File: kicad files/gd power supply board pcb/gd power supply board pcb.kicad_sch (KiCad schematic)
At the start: 16 parts

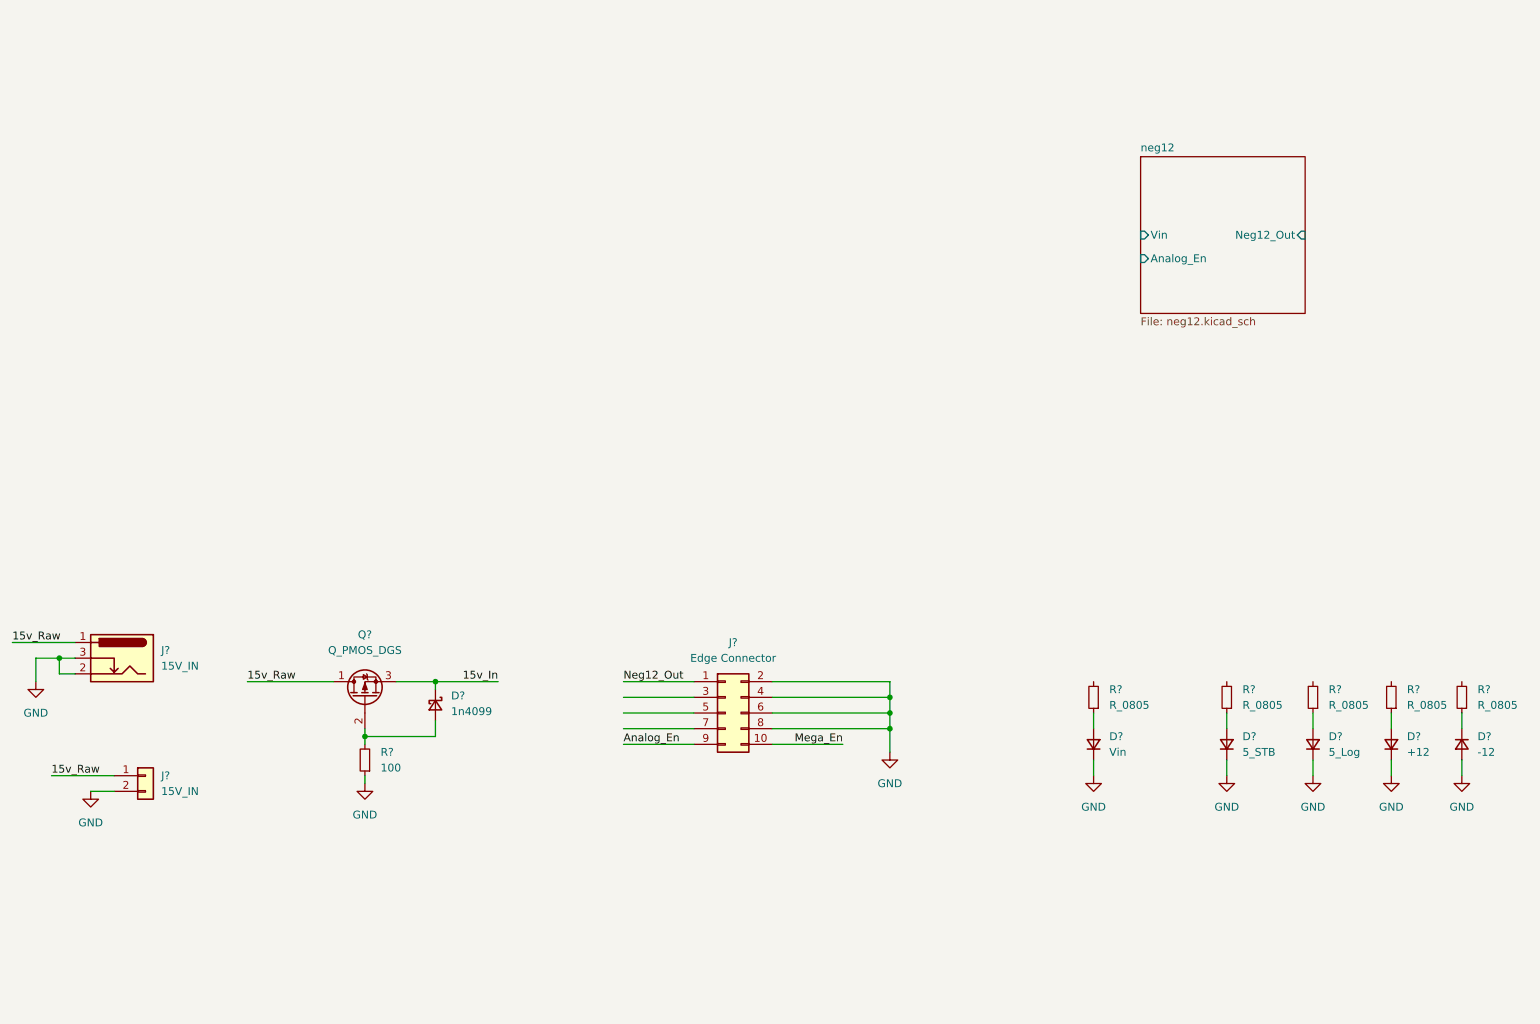
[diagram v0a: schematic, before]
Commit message: added 12v circuit with 34063 switcher
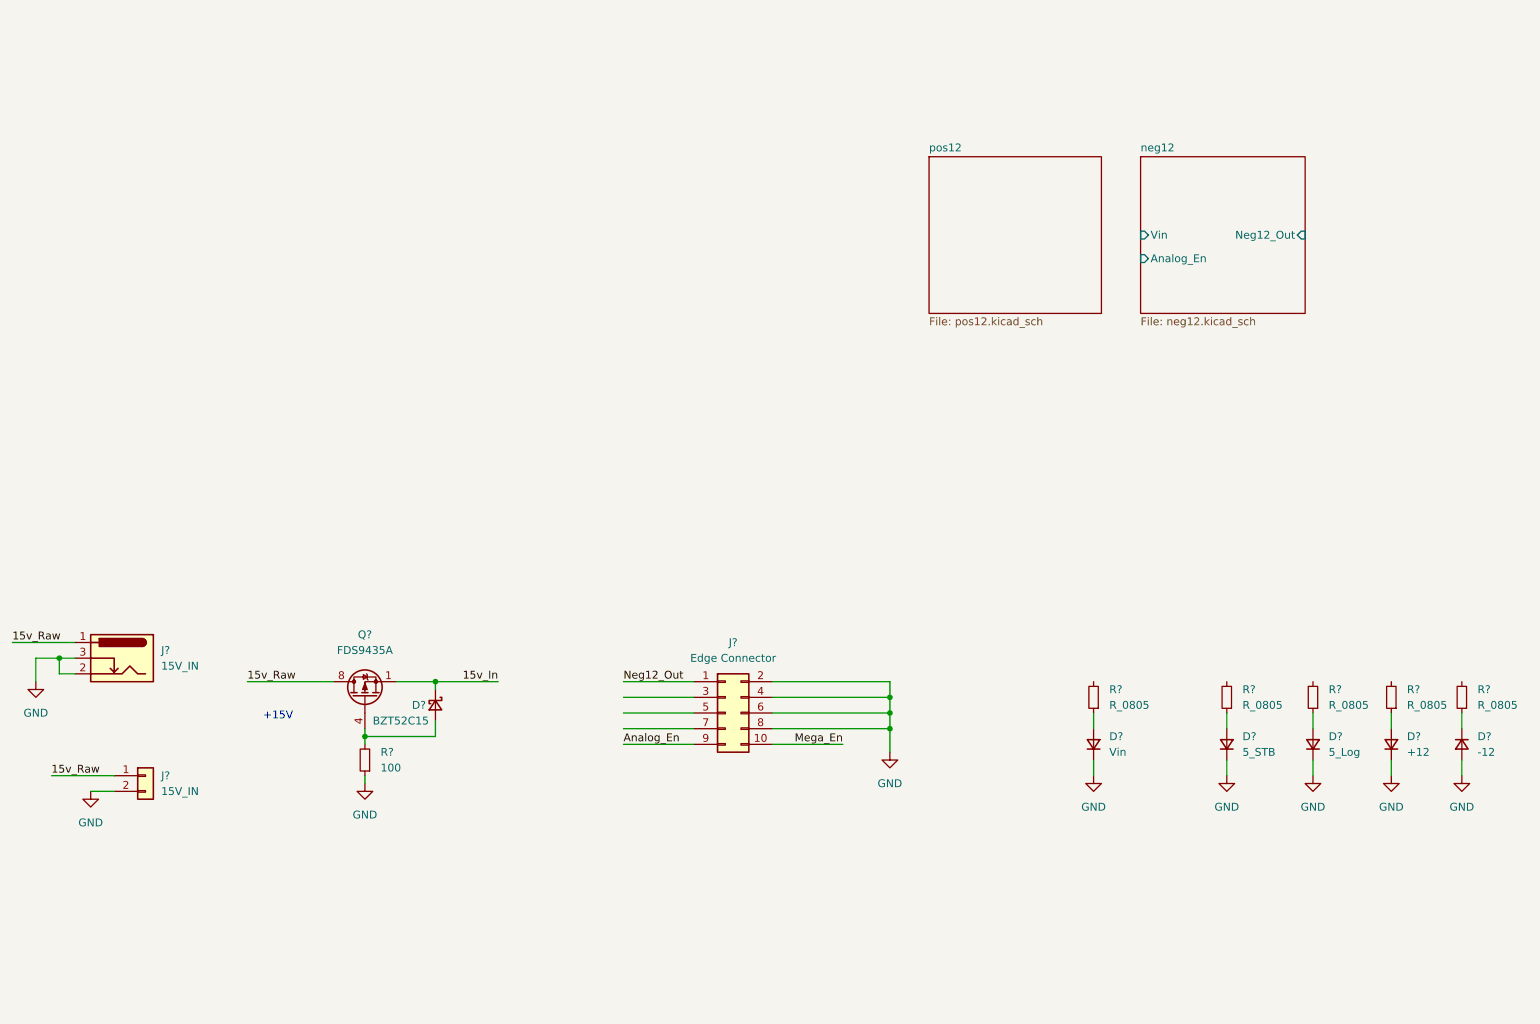
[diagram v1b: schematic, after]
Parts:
- removed Q?: Q_PMOS_DGS, symbol Device:Q_PMOS_DGS
- added Q?: FDS9435A, Package_SO:SOIC-8_3.9x4.9mm_P1.27mm, symbol Transistor_FET:FDS9435A
- D?: value 1n4099 -> BZT52C15; footprint (none) -> Diode_SMD:D_SOD-123
- J?: footprint (none) -> Connector_PinHeader_2.54mm:PinHeader_1x02_P2.54mm_Vertical
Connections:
- net 15v_In: now also Q?.1 (S), Q?.2 (S), Q?.3 (S)
- net 15v_Raw: now also Q?.5 (D), Q?.6 (D), Q?.7 (D), Q?.8 (D)
- net at D?.2 (A), R?.2: now also Q?.4 (G)
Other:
- added sheet pos12 (pos12.kicad_sch)
- note added: "+15V"

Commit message: cleaned up labels and footprints
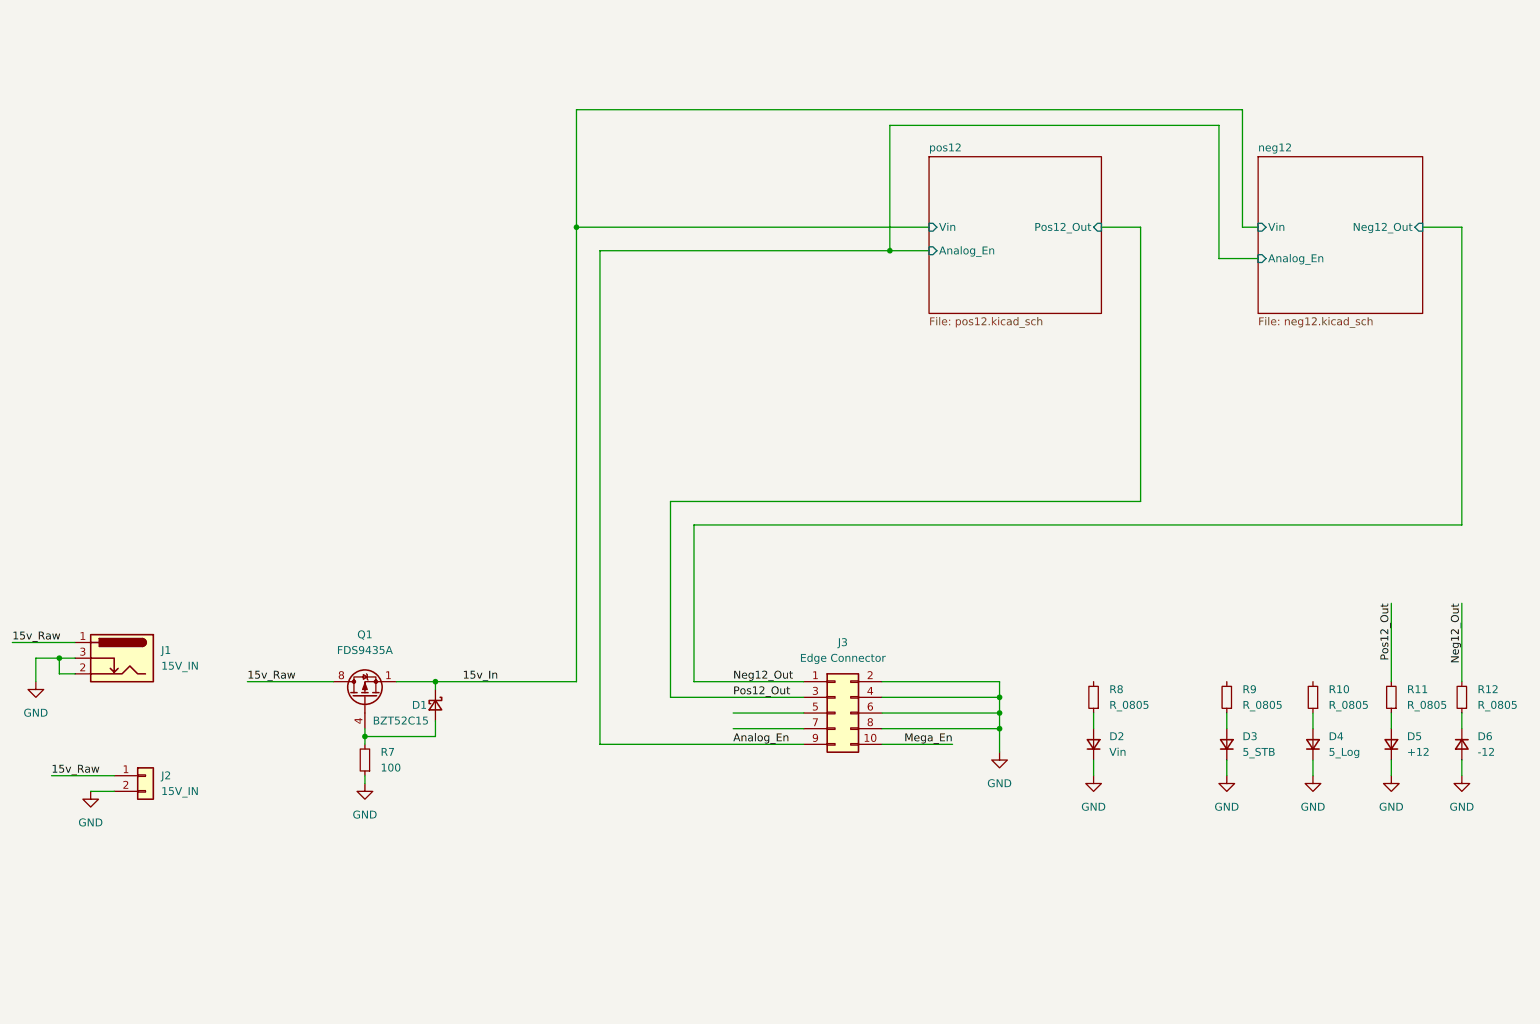
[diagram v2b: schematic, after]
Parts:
- gave numbers to parts that had none: 16
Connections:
- net Neg12_Out: now also R12.2
- net Pos12_Out: now reaches J3.3 (Pin_3)
- net Pos12_Out: now also R11.2
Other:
- sheet pos12 ports: added Analog_En, Pos12_Out, Vin; removed none
- note removed: "+15V"
- moved on the sheet: J3

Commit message: supply schematics done
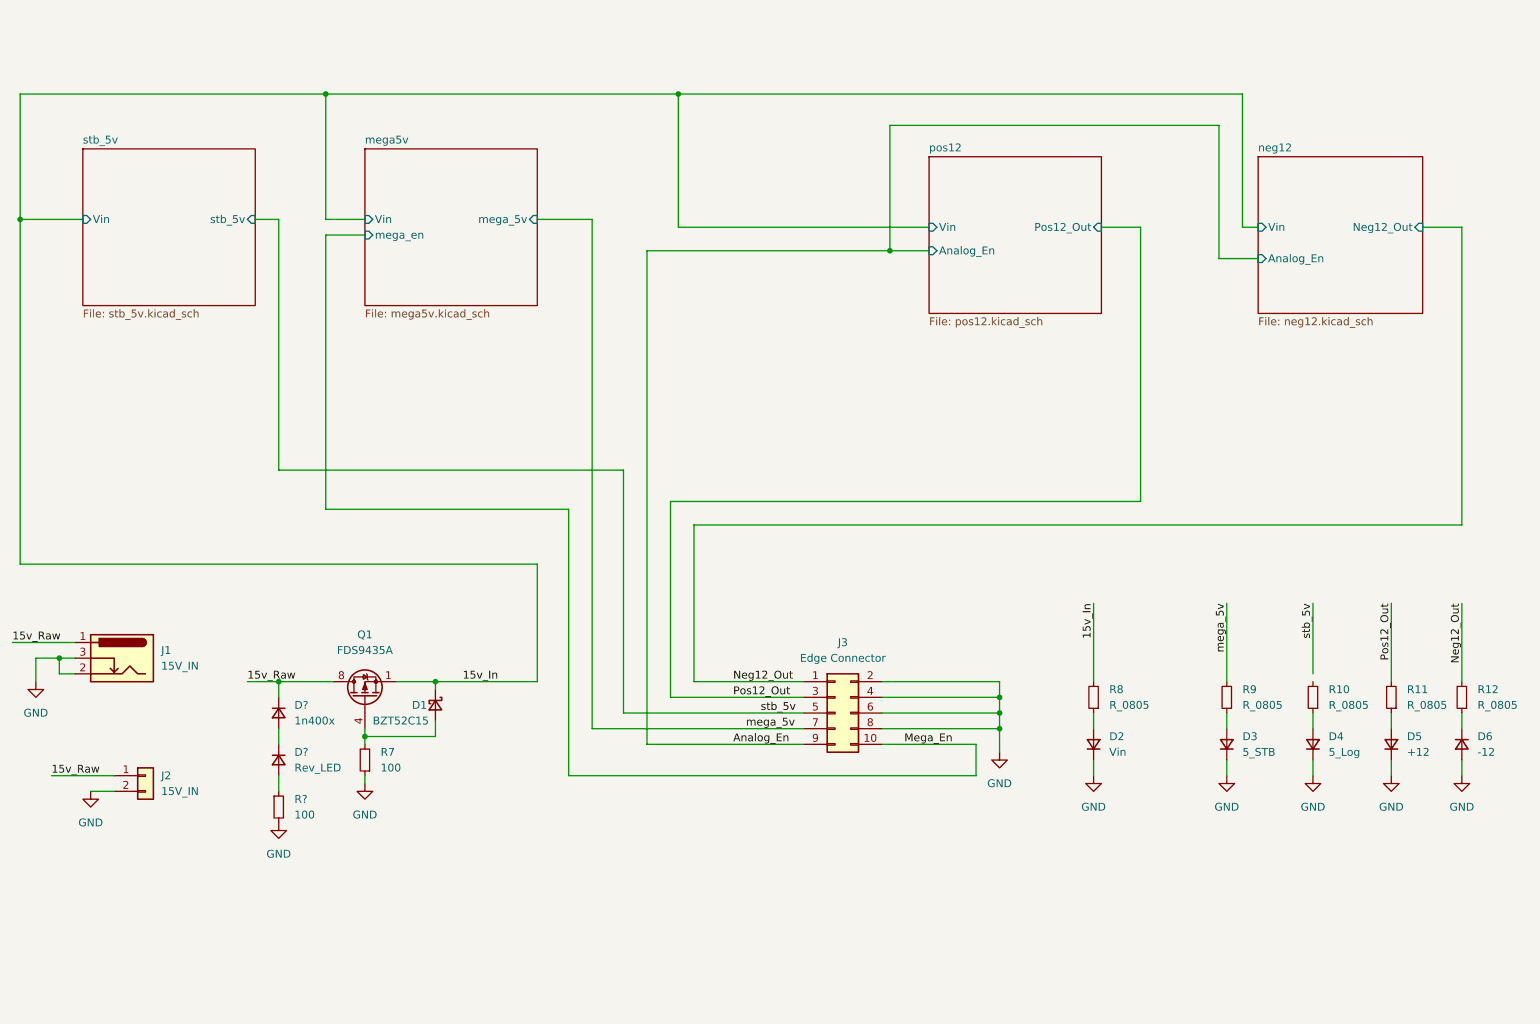
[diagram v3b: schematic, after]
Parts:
- added D?: Rev_LED, LED_SMD:LED_1206_3216Metric, symbol My Library:D_1206
- added D?: 1n400x, Diode_SMD:D_SMA, symbol My Library:D_1206
- added R?: 100, Resistor_SMD:R_0805_2012Metric, symbol My Library:R_0805
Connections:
- net 15v_In: now also R8.2
- net 15v_Raw: now also D?.1 (K)
- net GND: now also R?.2
- net mega_5v: now reaches R9.2
- net mega_5v: now also J3.7 (Pin_7)
- net stb_5v: now reaches J3.5 (Pin_5)
- new net: D?.1 (K), D?.2 (A)
- new net: D?.2 (A), R?.1
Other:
- added sheet mega5v (mega5v.kicad_sch)
- added sheet stb_5v (stb_5v.kicad_sch)

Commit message: before erc
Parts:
- J3: footprint (none) -> My Libraries:12pos-edge-2.54mm; symbol Connector_Generic:Conn_02x05_Odd_Even -> Connector_Generic:Conn_02x06_Odd_Even
- R21: renamed from R?; value 100 -> 1k
- gave numbers to parts that had none: 2
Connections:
- net Analog_En: now also J3.11 (Pin_11); no longer J3.9 (Pin_9)
- net Mega_En: now also J3.12 (Pin_12); no longer J3.10 (Pin_10)
- no-connect marks 0 -> 2

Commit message: initial floor planning done
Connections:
- net 15v_In: no longer D1.1 (K), Q1.1 (S), Q1.2 (S), Q1.3 (S)
- net stb_5v: now also R10.2
- new net Vin: D1.1 (K), Q1.1 (S), Q1.2 (S), Q1.3 (S)
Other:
- sheet mega5v ports: added Mega_En; removed mega_en
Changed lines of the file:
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@@
     (stroke (width 0) (type default) (color 0 0 0 0))
   )
-  (wire (pts (xy 231.14 118.11) (xy 231.14 129.54))
+  (wire (pts (xy 231.14 118.11) (xy 231.14 130.81))
     (stroke (width 0) (type default) (color 0 0 0 0))
   )
@@
     (effects (font (size 1.27 1.27)) (justify right bottom))
   )
-  (label "15v_In" (at 99.06 130.81 180)
+  (label "Vin" (at 99.06 130.81 180)
     (effects (font (size 1.27 1.27)) (justify right bottom))
   )
@@
       (effects (font (size 1.27 1.27)) (justify right))
     )
-    (pin "mega_en" input (at 77.47 58.42 180)
+    (pin "Mega_En" input (at 77.47 58.42 180)
       (effects (font (size 1.27 1.27)) (justify left))
     )
@@
       (reference "#PWR0118") (unit 1) (value "GND") (footprint "")
     )
-    (path "/fc065b92-de59-4c29-93b4-0f722018f063/3aced845-83c1-4b5c-906f-7a1884062712"
-      (reference "#PWR0119") (unit 1) (value "GND") (footprint "")
-    )
     (path "/fc065b92-de59-4c29-93b4-0f722018f063/c35a082e-733e-4427-b04c-9802e85913c2"
       (reference "#PWR0120") (unit 1) (value "GND") (footprint "")
@@
       (reference "C8") (unit 1) (value "470p") (footprint "Capacitor_SMD:C_0603_1608Metric")
     )
-    (path "/fc065b92-de59-4c29-93b4-0f722018f063/f1bdf1bc-4795-4c22-8f8f-6d8bee3b843c"
-      (reference "C9") (unit 1) (value "120u / 5v") (footprint "Capacitor_SMD:C_0805_2012Metric")
-    )
     (path "/fc065b92-de59-4c29-93b4-0f722018f063/c574b3be-f25a-4a58-9138-6a3766aa0952"
       (reference "C10") (unit 1) (value "10u") (footprint "Capacitor_SMD:C_0805_2012Metric")
@@
       (reference "TP15") (unit 1) (value "TestPoint_Harwin") (footprint "My Libraries:Harwin-S1751-46-Test-Point")
     )
-    (path "/fc065b92-de59-4c29-93b4-0f722018f063/3e965d51-c950-44e4-aade-2d3ffcc7a1b7"
-      (reference "TP16") (unit 1) (value "TestPoint_Harwin") (footprint "My Libraries:Harwin-S1751-46-Test-Point")
-    )
     (path "/fc065b92-de59-4c29-93b4-0f722018f063/fdd7c921-6762-400c-b95b-67325b144a1d"
